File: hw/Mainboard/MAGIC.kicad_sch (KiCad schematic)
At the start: 19 parts, among them SW1 RESET, SW4 NMI, U18 SN74LVC4245APWR, U19 SN74LVC4245APWR, U20 SN74LVC4245APWR

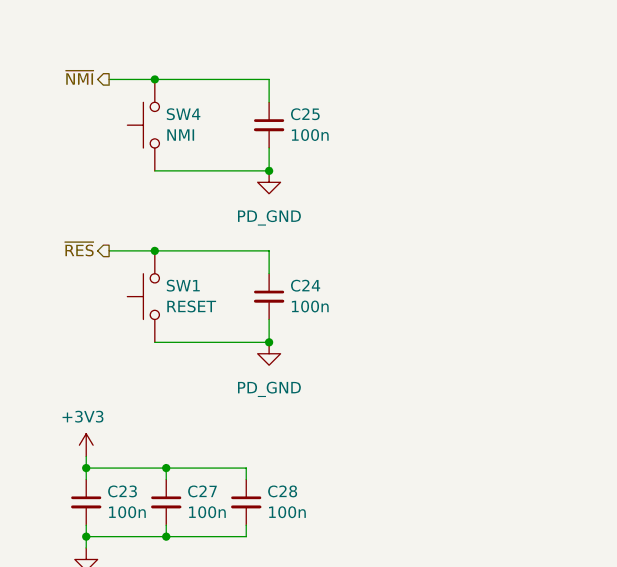
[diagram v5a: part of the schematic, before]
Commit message: hw: pull cbus0 high
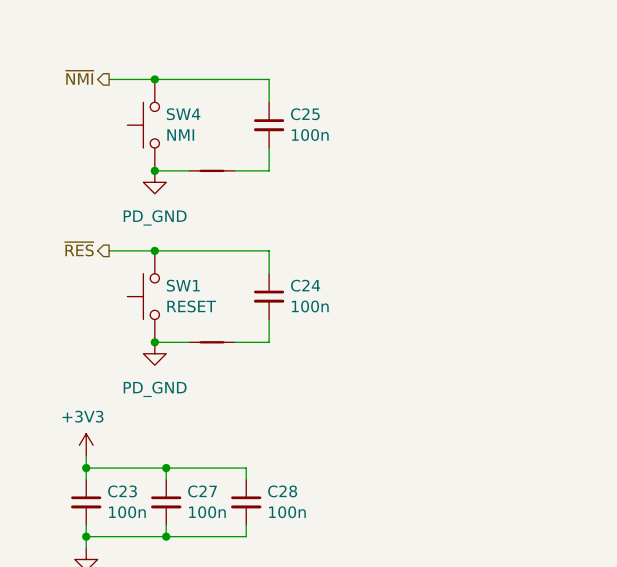
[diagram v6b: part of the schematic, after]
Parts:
- added NT22, NT23: GND, PET:NetTie-2_SMD_Pad_1.6_to_0.4mm, symbol Device:NetTie_2
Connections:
- net PD_GND: now also NT22.1, NT23.1; no longer C24.2, C25.2
- new net: C24.2, NT23.2
- new net: C25.2, NT22.2
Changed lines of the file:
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@@
   (junction (at 232.41 52.07) (diameter 0) (color 0 0 0 0)
   )
-  (junction (at 39.37 140.97) (diameter 0) (color 0 0 0 0)
-  )
   (junction (at 27.94 175.26) (diameter 0) (color 0 0 0 0)
   )
@@
   (junction (at 19.05 154.94) (diameter 0) (color 0 0 0 0)
   )
+  (junction (at 26.67 121.92) (diameter 0) (color 0 0 0 0)
+  )
+  (junction (at 26.67 140.97) (diameter 0) (color 0 0 0 0)
+  )
   (junction (at 201.93 41.91) (diameter 0) (color 0 0 0 0)
   )
@@
   )
   (junction (at 245.11 76.2) (diameter 0) (color 0 0 0 0)
-  )
-  (junction (at 39.37 121.92) (diameter 0) (color 0 0 0 0)
   )
   (junction (at 26.67 130.81) (diameter 0) (color 0 0 0 0)
@@
     (stroke (width 0) (type default) (color 0 0 0 0))
   )
-  (wire (pts (xy 26.67 121.92) (xy 39.37 121.92))
-    (stroke (width 0) (type default) (color 0 0 0 0))
-  )
   (bus (pts (xy 177.165 44.45) (xy 167.005 44.45))
     (stroke (width 0) (type default) (color 0 0 0 0))
@@
     (stroke (width 0) (type default) (color 0 0 0 0))
   )
+  (wire (pts (xy 35.56 121.92) (xy 39.37 121.92))
+    (stroke (width 0) (type default) (color 0 0 0 0))
+  )
   (bus (pts (xy 267.97 93.98) (xy 267.97 96.52))
     (stroke (width 0) (type default) (color 0 0 0 0))
@@
     (stroke (width 0) (type default) (color 0 0 0 0))
   )
+  (wire (pts (xy 26.67 121.92) (xy 30.48 121.92))
+    (stroke (width 0) (type default) (color 0 0 0 0))
+  )
   (bus (pts (xy 267.97 91.44) (xy 267.97 93.98))
     (stroke (width 0) (type default) (color 0 0 0 0))
@@
     (stroke (width 0) (type default) (color 0 0 0 0))
   )
+  (wire (pts (xy 35.56 140.97) (xy 39.37 140.97))
+    (stroke (width 0) (type default) (color 0 0 0 0))
+  )
   (wire (pts (xy 102.87 63.5) (xy 109.22 63.5))
     (stroke (width 0) (type default) (color 0 0 0 0))
   )
-  (wire (pts (xy 26.67 140.97) (xy 39.37 140.97))
-    (stroke (width 0) (type default) (color 0 0 0 0))
-  )
   (wire (pts (xy 139.7 67.31) (xy 154.94 67.31))
     (stroke (width 0) (type default) (color 0 0 0 0))
@@
   )
   (wire (pts (xy 102.87 83.82) (xy 109.22 83.82))
+    (stroke (width 0) (type default) (color 0 0 0 0))
+  )
+  (wire (pts (xy 26.67 140.97) (xy 30.48 140.97))
     (stroke (width 0) (type default) (color 0 0 0 0))
   )
@@
     (pin "2")
   )
-  (symbol (lib_id "PET:PD_GND") (at 39.37 121.92 0) (unit 1)
+  (symbol (lib_id "PET:PD_GND") (at 26.67 121.92 0) (unit 1)
     (in_bom yes) (on_board yes) (fields_autoplaced)
-    (property "Reference" "#PWR0141" (id 0) (at 39.37 128.27 0)
-      (effects (font (size 1.27 1.27)) hide)
-    )
-    (property "Value" "PD_GND" (id 1) (at 39.37 127 0))
-    (property "Footprint" "" (id 2) (at 39.37 121.92 0)
-      (effects (font (size 1.27 1.27)) hide)
-    )
-    (property "Datasheet" "" (id 3) (at 39.37 121.92 0)
-      (effects (font (size 1.27 1.27)) hide)
-    )
-    (pin "1")
+    (property "Reference" "#PWR0141" (id 0) (at 26.67 128.27 0)
+      (effects (font (size 1.27 1.27)) hide)
+    )
+    (property "Value" "PD_GND" (id 1) (at 26.67 127 0))
+    (property "Footprint" "" (id 2) (at 26.67 121.92 0)
+      (effects (font (size 1.27 1.27)) hide)
+    )
+    (property "Datasheet" "" (id 3) (at 26.67 121.92 0)
+      (effects (font (size 1.27 1.27)) hide)
+    )
+    (pin "1")
+  )
+  (symbol (lib_id "Device:NetTie_2") (at 33.02 140.97 0) (unit 1)
+    (in_bom yes) (on_board yes) (fields_autoplaced)
+    (property "Reference" "NT23" (id 0) (at 33.02 135.89 0)
+      (effects (font (size 1.27 1.27)) hide)
+    )
+    (property "Value" "GND" (id 1) (at 33.02 138.43 0)
+      (effects (font (size 1.27 1.27)) hide)
+    )
+    (property "Footprint" "PET:NetTie-2_SMD_Pad_1.6_to_0.4mm" (id 2) (at 33.02 140.97 0)
+      (effects (font (size 1.27 1.27)) hide)
+    )
+    (property "Datasheet" "~" (id 3) (at 33.02 140.97 0)
+      (effects (font (size 1.27 1.27)) hide)
+    )
+    (pin "1")
+    (pin "2")
   )
   (symbol (lib_id "Device:R_Small") (at 159.385 139.7 90) (unit 1)
@@
     (pin "2")
   )
+  (symbol (lib_id "Device:NetTie_2") (at 33.02 121.92 0) (unit 1)
+    (in_bom yes) (on_board yes) (fields_autoplaced)
+    (property "Reference" "NT22" (id 0) (at 33.02 116.84 0)
+      (effects (font (size 1.27 1.27)) hide)
+    )
+    (property "Value" "GND" (id 1) (at 33.02 119.38 0)
+      (effects (font (size 1.27 1.27)) hide)
+    )
+    (property "Footprint" "PET:NetTie-2_SMD_Pad_1.6_to_0.4mm" (id 2) (at 33.02 121.92 0)
+      (effects (font (size 1.27 1.27)) hide)
+    )
+    (property "Datasheet" "~" (id 3) (at 33.02 121.92 0)
+      (effects (font (size 1.27 1.27)) hide)
+    )
+    (pin "1")
+    (pin "2")
+  )
   (symbol (lib_id "Device:R_Small") (at 146.05 143.51 0) (unit 1)
     (in_bom yes) (on_board yes)
@@
     (pin "2")
   )
-  (symbol (lib_id "PET:PD_GND") (at 39.37 140.97 0) (unit 1)
+  (symbol (lib_id "PET:PD_GND") (at 26.67 140.97 0) (unit 1)
     (in_bom yes) (on_board yes) (fields_autoplaced)
-    (property "Reference" "#PWR0159" (id 0) (at 39.37 147.32 0)
-      (effects (font (size 1.27 1.27)) hide)
-    )
-    (property "Value" "PD_GND" (id 1) (at 39.37 146.05 0))
-    (property "Footprint" "" (id 2) (at 39.37 140.97 0)
-      (effects (font (size 1.27 1.27)) hide)
-    )
-    (property "Datasheet" "" (id 3) (at 39.37 140.97 0)
-      (effects (font (size 1.27 1.27)) hide)
-    )
+    (property "Reference" "#PWR0159" (id 0) (at 26.67 147.32 0)
+      (effects (font (size 1.27 1.27)) hide)
+    )
+    (property "Value" "PD_GND" (id 1) (at 26.67 146.05 0))
+    (property "Footprint" "" (id 2) (at 26.67 140.97 0)
+      (effects (font (size 1.27 1.27)) hide)
+    )
+    (property "Datasheet" "" (id 3) (at 26.67 140.97 0)
+      (effects (font (size 1.27 1.27)) hide)
+    )

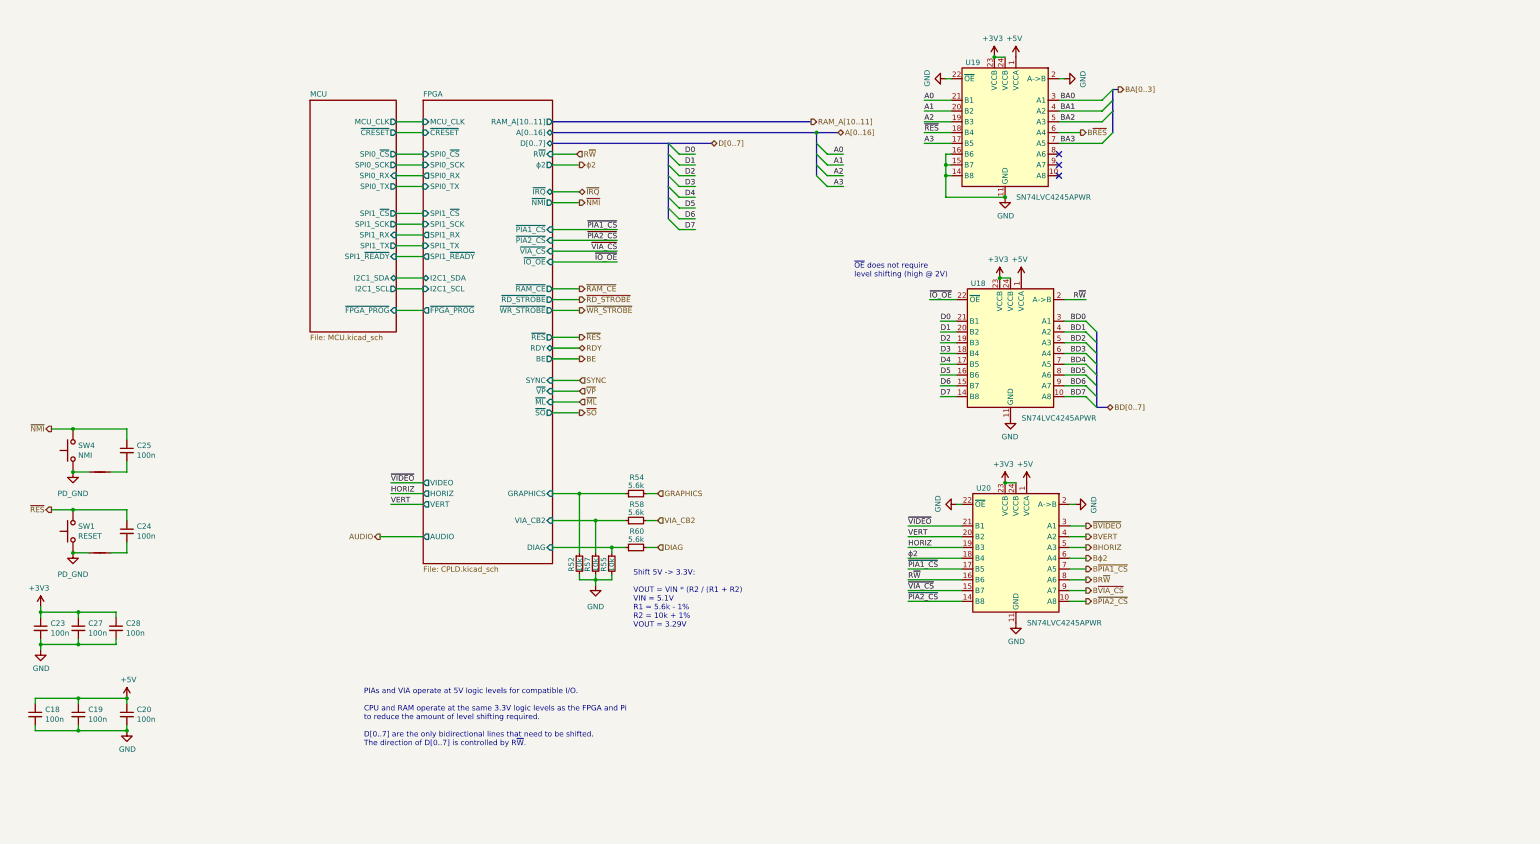
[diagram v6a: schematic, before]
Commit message: hw: larger schematic pages, routed w/netties
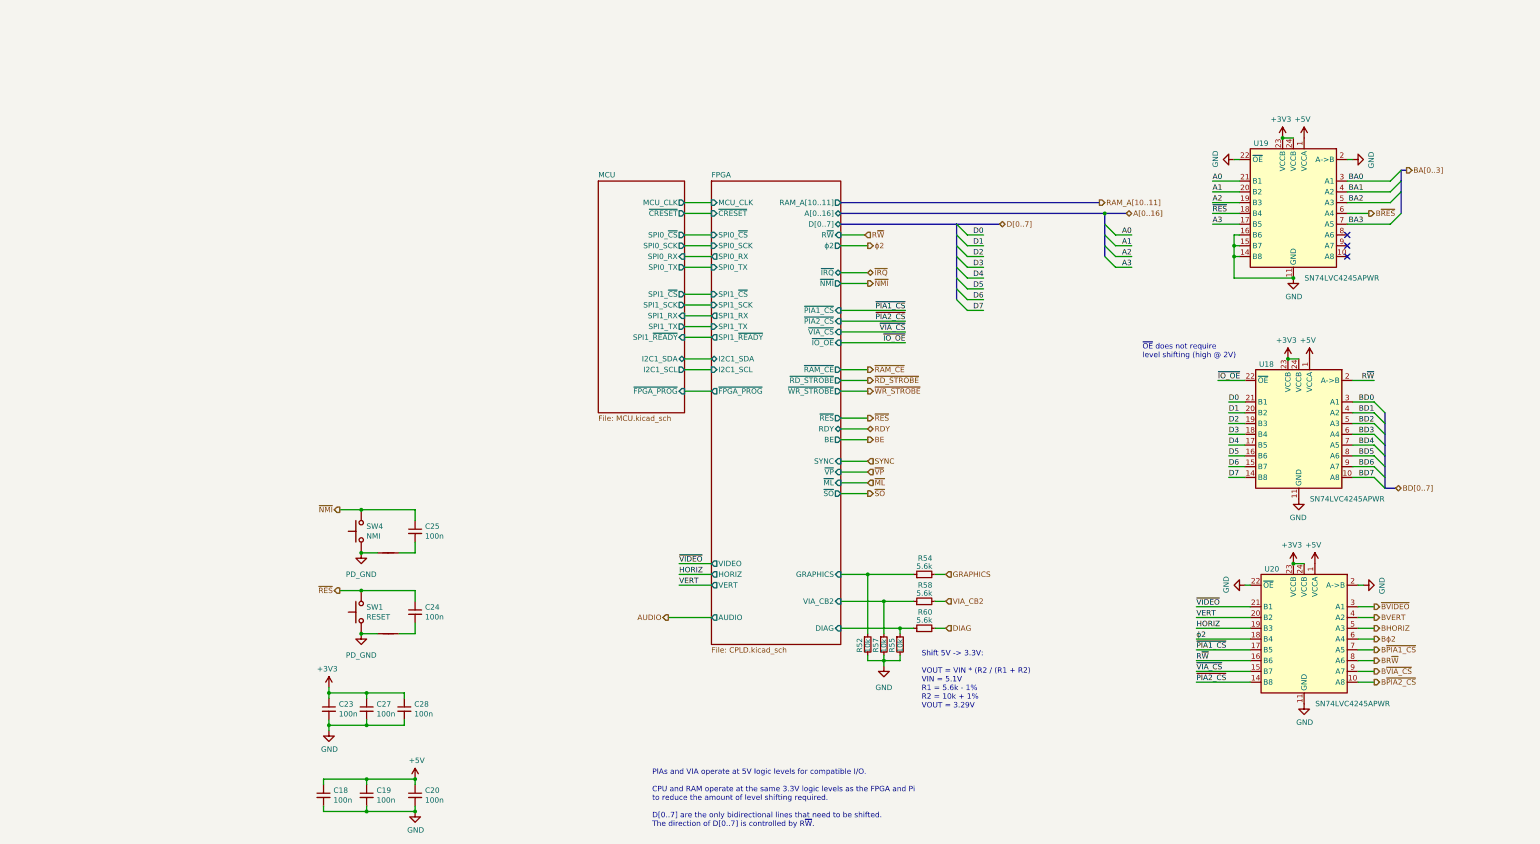
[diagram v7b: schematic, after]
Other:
- moved on the sheet: C18, C19, C20, C23, C24, C25, C27, C28, R52, R54, R55, R57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

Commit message: hw: wip
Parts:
- added NT32, NT36: +5V, PET:NetTie-2_SMD_Pad_1.6_to_0.4mm, symbol PET:PowerTie_2
- NT22, NT23: symbol Device:NetTie_2 -> PET:PowerTie_2
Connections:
- net +5V: no longer names the net of C18.1, C20.1, U18.1 (VCCA), U19.1 (VCCA)
- net +5V: now also NT32.2; no longer C19.1, U20.1 (VCCA)
- new net: C19.1, NT36.2, U20.1 (VCCA)
- new net PD_5V: NT32.1, NT36.1
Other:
- sheet FPGA ports: added MCU_CEC, ~{SPI_ENA}; removed ~{FPGA_PROG}
- sheet MCU ports: added MCU_CEC, ~{SPI_ENA}; removed ~{FPGA_PROG}
- moved on the sheet: C18, C19, C20, R52, R54, R55, R57, R58, R60, U18, U19, U20
